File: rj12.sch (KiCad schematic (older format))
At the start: 2 parts, among them J1 Conn_02x06_Top_Bottom, P1 RJ12_Housing

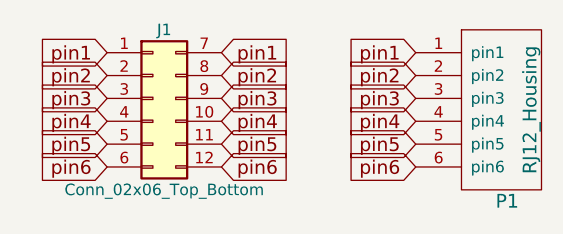
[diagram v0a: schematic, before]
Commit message: Re-design the rj12 housing
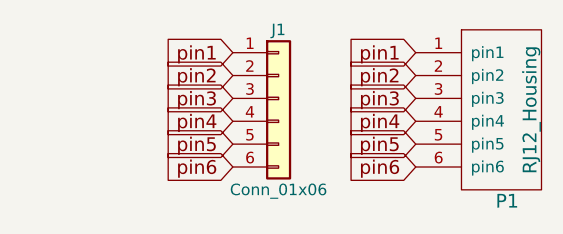
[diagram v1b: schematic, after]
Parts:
- removed J1: Conn_02x06_Top_Bottom, rj12connector:2x6PinHeader, symbol Conn_02x06_Top_Bottom
- added J1: Conn_01x06, Pin_Headers:Pin_Header_Straight_1x06_Pitch2.54mm, symbol Conn_01x06
- P1: footprint rj12connector:myRJ12 -> RJ12-Housing:RJ12
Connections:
- net pin1: now also J1.1 (Pin_1)
- net pin2: now also J1.2 (Pin_2)
- net pin3: now also J1.3 (Pin_3)
- net pin4: now also J1.4 (Pin_4)
- net pin5: now also J1.5 (Pin_5)
- net pin6: now also J1.6 (Pin_6)
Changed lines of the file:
@@
 LIBS:valves
 LIBS:RJ12-Housing
+LIBS:rj12-cache
 EELAYER 25 0
 EELAYER END
@@
 Comment4 ""
 $EndDescr
-$Comp
-L Conn_02x06_Top_Bottom J1
-U 1 1 59CCD3BF
-P 3850 2850
-F 0 "J1" H 3900 3150 50  0000 C CNN
-F 1 "Conn_02x06_Top_Bottom" H 3900 2450 50  0000 C CNN
-F 2 "rj12connector:2x6PinHeader" H 3850 2850 50  0001 C CNN
-F 3 "" H 3850 2850 50  0001 C CNN
-	1    3850 2850
-	1    0    0    -1
-$EndComp
-Text GLabel 3650 2650 0    60   Input ~ 0
+Text GLabel 4200 2650 0    60   Input ~ 0
 pin1
-Text GLabel 3650 2750 0    60   Input ~ 0
+Text GLabel 4200 2750 0    60   Input ~ 0
 pin2
-Text GLabel 3650 2850 0    60   Input ~ 0
+Text GLabel 4200 2850 0    60   Input ~ 0
 pin3
-Text GLabel 3650 2950 0    60   Input ~ 0
+Text GLabel 4200 2950 0    60   Input ~ 0
 pin4
-Text GLabel 3650 3050 0    60   Input ~ 0
+Text GLabel 4200 3050 0    60   Input ~ 0
 pin5
-Text GLabel 3650 3150 0    60   Input ~ 0
+Text GLabel 4200 3150 0    60   Input ~ 0
 pin6
-Text GLabel 4150 2650 2    60   Input ~ 0
-pin1
-Text GLabel 4150 2750 2    60   Input ~ 0
-pin2
-Text GLabel 4150 2850 2    60   Input ~ 0
-pin3
-Text GLabel 4150 2950 2    60   Input ~ 0
-pin4
-Text GLabel 4150 3050 2    60   Input ~ 0
-pin5
-Text GLabel 4150 3150 2    60   Input ~ 0
-pin6
-$Comp
-L RJ12_Housing P1
-U 1 1 59CCD932
-P 5350 2950
-F 0 "P1" H 5400 2600 60  0000 C CNN
-F 1 "RJ12_Housing" V 5500 3000 60  0000 C CNN
-F 2 "rj12connector:myRJ12" V 5450 3050 60  0001 C CNN
-F 3 "" V 5450 3050 60  0001 C CNN
-	1    5350 2950
-	1    0    0    -1
-$EndComp
 Text GLabel 5000 2650 0    60   Input ~ 0
 pin1
@@
 Text GLabel 5000 3150 0    60   Input ~ 0
 pin6
+$Comp
+L Conn_01x06 J1
+U 1 1 59DF5F34
+P 4400 2850
+F 0 "J1" H 4400 3150 50  0000 C CNN
+F 1 "Conn_01x06" H 4400 2450 50  0000 C CNN
+F 2 "Pin_Headers:Pin_Header_Straight_1x06_Pitch2.54mm" H 4400 2850 50  0001 C CNN
+F 3 "" H 4400 2850 50  0001 C CNN
+	1    4400 2850
+	1    0    0    -1
+$EndComp
+$Comp
+L RJ12_Housing P1
+U 1 1 59DF6F57
+P 5350 2950
+F 0 "P1" H 5400 2600 60  0000 C CNN
+F 1 "RJ12_Housing" V 5500 3000 60  0000 C CNN
+F 2 "RJ12-Housing:RJ12" V 5450 3050 60  0001 C CNN
+F 3 "" V 5450 3050 60  0001 C CNN
+	1    5350 2950
+	1    0    0    -1
+$EndComp
 $EndSCHEMATC
